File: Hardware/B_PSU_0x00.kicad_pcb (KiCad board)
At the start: 2 copper layers, 111.8 x 73.7 mm, 95 parts, among them J1 Conn_01x03, J10 Conn_01x02, J11 Conn_01x02, J12 Conn_01x02, J13 Conn_01x02, J14 Conn_01x02, J15 Conn_01x03, J16 Conn_01x03, J17 Conn_01x03, J18 Conn_01x04, J19 Conn_01x04, J2 Conn_01x04, J3 Conn_01x04, J4 Conn_01x02, J5 Conn_01x02, J6 Conn_01x02, J7 Conn_01x03, J8 Conn_01x02, J9 Conn_01x03, U1 ADP5070AREZ, U2 ADP7142AUJZ-5.0, U3 ADP7142AUJZ-3.3, U4 ADP7142AUJZ-1.8, U5 ADP7182AUJZ-1.8, U6 ADP7142AUJZ-2.5, U7 ADP7183ACPZN3.3-R7

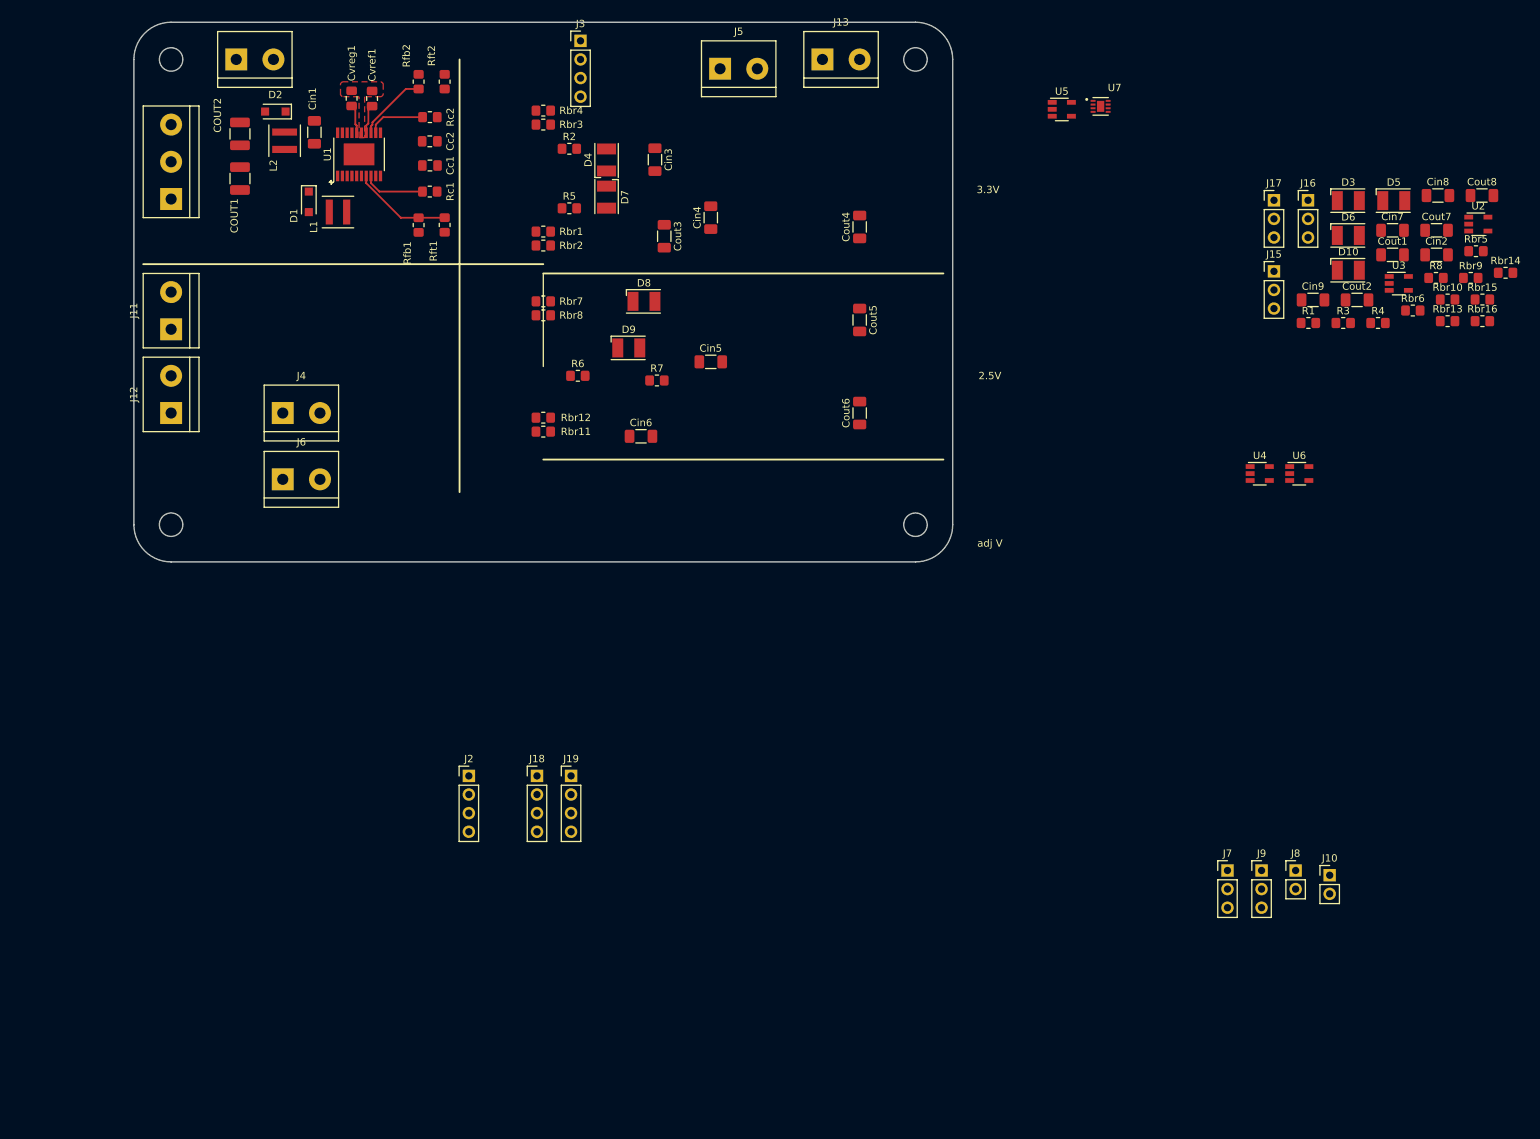
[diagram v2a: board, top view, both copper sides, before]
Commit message: updated to sch and pcb
correct LDO ic's and board outline
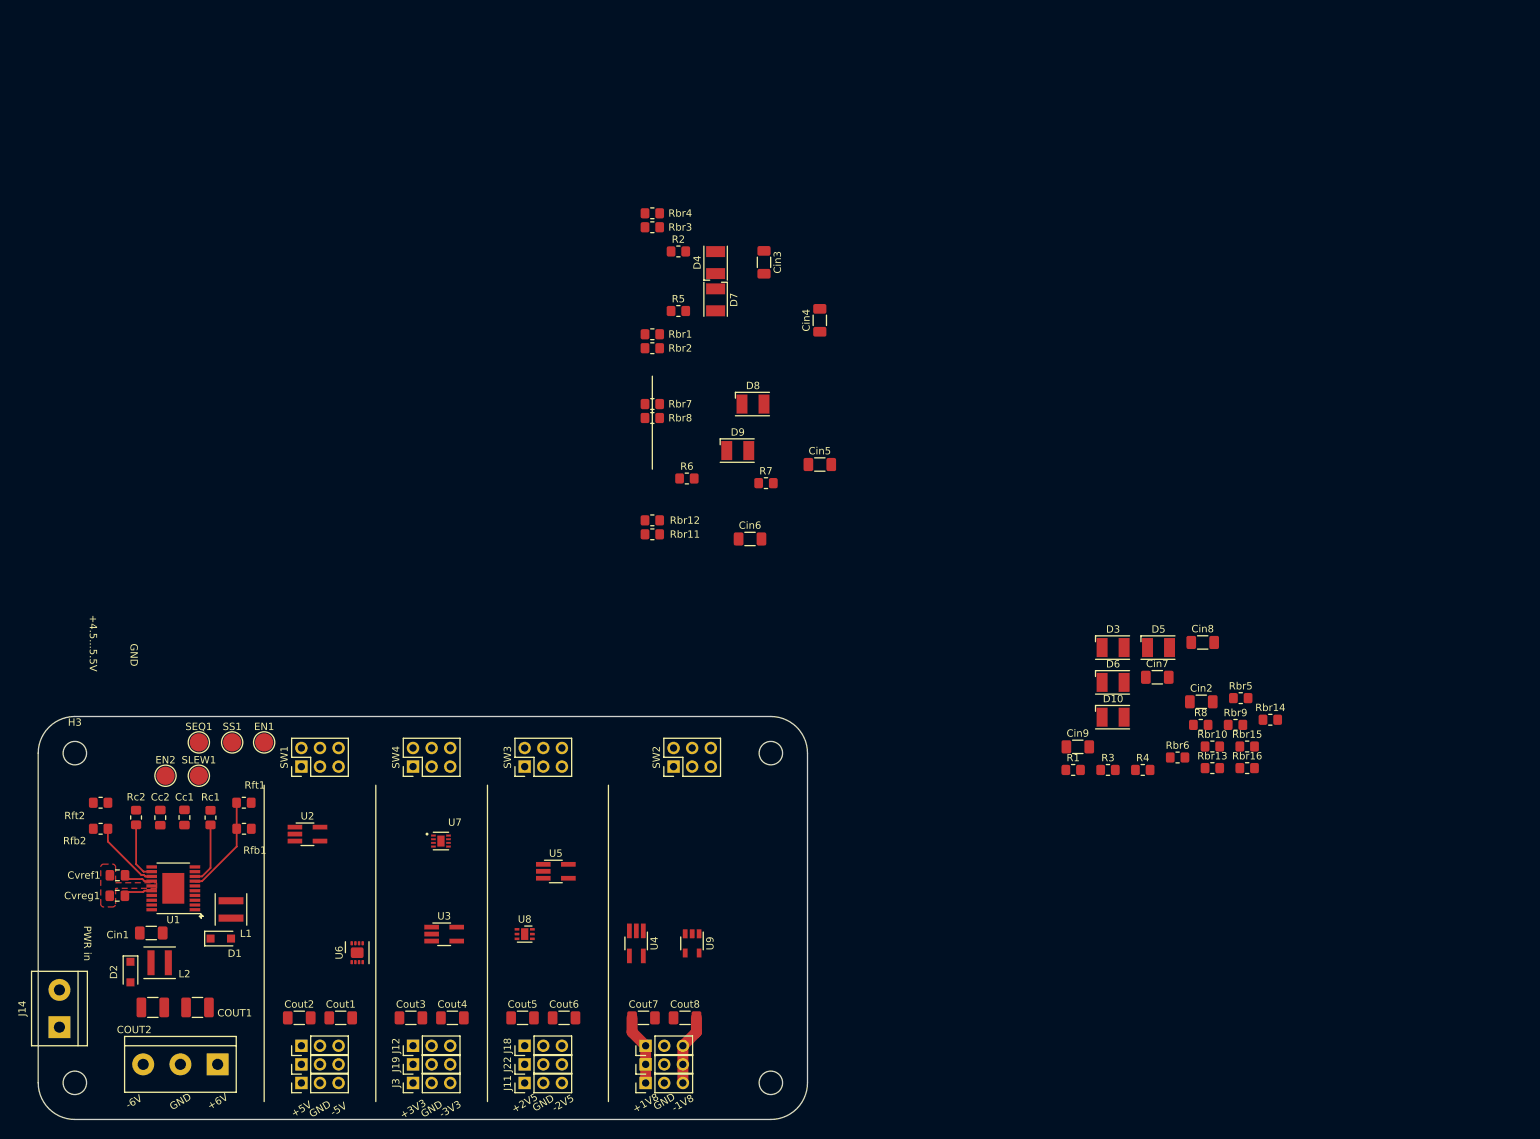
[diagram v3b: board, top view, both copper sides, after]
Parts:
- removed H5: MountingHole, MountingHole:MountingHole_3.2mm_M3
- removed J10, J8: Conn_01x02, Connector_PinHeader_2.54mm:PinHeader_1x02_P2.54mm_Vertical
- removed J15, J16, J17, J7, J9: Conn_01x03, Connector_PinHeader_2.54mm:PinHeader_1x03_P2.54mm_Vertical
- removed J2: Conn_01x04, Connector_PinHeader_2.54mm:PinHeader_1x04_P2.54mm_Vertical
- added EN1: TestPoint, TestPoint:TestPoint_Pad_D2.5mm, F.Cu at (53.3, 113.5)
- added EN2: TestPoint, TestPoint:TestPoint_Pad_D2.5mm, F.Cu at (39.9, 118.1)
- added H3: MountingHole, MountingHole:MountingHole_3.2mm_M3, F.Cu at (27.5, 115.0)
- added J20: Conn_01x03, Connector_PinHeader_2.54mm:PinHeader_1x03_P2.54mm_Vertical, F.Cu at (58.4, 154.9)
- added J21: Conn_01x03, Connector_PinHeader_2.54mm:PinHeader_1x03_P2.54mm_Vertical, F.Cu at (105.4, 154.9)
- added J22: Conn_01x03, Connector_PinHeader_2.54mm:PinHeader_1x03_P2.54mm_Vertical, F.Cu at (88.9, 157.5)
- added SEQ1: TestPoint, TestPoint:TestPoint_Pad_D2.5mm, F.Cu at (44.4, 113.5)
- added SLEW1: TestPoint, TestPoint:TestPoint_Pad_D2.5mm, F.Cu at (44.4, 118.1)
- added SS1: TestPoint, TestPoint:TestPoint_Pad_D2.5mm, F.Cu at (49.0, 113.5)
- added SW1: SW_DPDT_x2, Connector_PinHeader_2.54mm:PinHeader_2x03_P2.54mm_Vertical, F.Cu at (58.4, 116.8)
- added SW2: SW_DPDT_x2, Connector_PinHeader_2.54mm:PinHeader_2x03_P2.54mm_Vertical, F.Cu at (109.2, 116.8)
- added SW3: SW_DPDT_x2, Connector_PinHeader_2.54mm:PinHeader_2x03_P2.54mm_Vertical, F.Cu at (88.9, 116.8)
- added SW4: SW_DPDT_x2, Connector_PinHeader_2.54mm:PinHeader_2x03_P2.54mm_Vertical, F.Cu at (73.7, 116.8)
- added U8: ADP7182ACPZN-2.5R7, Package_DFN_QFN:DFN-6-1EP_2x2mm_P0.65mm_EP1x1.6mm, F.Cu at (88.9, 139.7)
- added U9: ADP7182AUJZ-1.8, Package_TO_SOT_SMD:TSOT-23-5, F.Cu at (111.8, 141.0)
- Cin4: value 10uF -> 4.7uF
- Cout4: value 2.2uF -> 4.7uF
- J11, J12, J13, J4, J5, J6: value Conn_01x02 -> Conn_01x03; footprint TerminalBlock:TerminalBlock_bornier-2_P5.08mm -> Connector_PinHeader_2.54mm:PinHeader_1x03_P2.54mm_Vertical
- J18, J19, J3: value Conn_01x04 -> Conn_01x03; footprint Connector_PinHeader_2.54mm:PinHeader_1x04_P2.54mm_Vertical -> Connector_PinHeader_2.54mm:PinHeader_1x03_P2.54mm_Vertical
- U2: value ADP7142AUJZ-5.0 -> ADP7118WAUJZ-5.0; footprint Package_TO_SOT_SMD:TSOT-23-5 -> Package_TO_SOT_SMD:TSOT-23-5_HandSoldering
- U3: value ADP7142AUJZ-3.3 -> ADP7118AUJZ-3.3-R7; footprint Package_TO_SOT_SMD:TSOT-23-5 -> Package_TO_SOT_SMD:TSOT-23-5_HandSoldering
- U4: footprint Package_TO_SOT_SMD:TSOT-23-5 -> Package_TO_SOT_SMD:TSOT-23-5_HandSoldering
- U5: value ADP7182AUJZ-1.8 -> ADP7118AUJZ-2.5-R7; footprint Package_TO_SOT_SMD:TSOT-23-5 -> Package_TO_SOT_SMD:TSOT-23-5_HandSoldering
- U6: value ADP7142AUJZ-2.5 -> ADP7182ACPZ-5.0-R7; footprint Package_TO_SOT_SMD:TSOT-23-5 -> Package_CSP:LFCSP-8-1EP_3x3mm_P0.5mm_EP1.45x1.74mm
- moved U2 180.2 mm to (59.2, 126.0)
- moved Cout1 177.4 mm to (63.8, 151.1)
- moved Cout2 174.5 mm to (58.1, 151.1)
- moved U3 157.7 mm to (77.9, 139.7)
- moved Cout8 156.3 mm to (110.8, 151.1)
- moved Cout7 152.5 mm to (105.1, 151.1)
- moved U6 144.3 mm to (66.0, 142.2), turned to 90 degrees
- moved J3 144.1 mm to (73.7, 160.0), turned to 90 degrees
- moved H1 141.1 mm to (122.5, 160.0)
- moved J13 139.3 mm to (105.4, 157.5), turned to 90 degrees
- moved J5 138.8 mm to (105.4, 160.0), turned to 90 degrees
- moved U7 134.8 mm to (77.5, 127.0)
- moved J14 134.3 mm to (25.4, 152.4), turned to 90 degrees
- moved U5 124.8 mm to (93.2, 131.1)
- moved Cout4 121.4 mm to (79.0, 151.1), turned to 0 degrees
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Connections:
- COUT1 pad 1: GNDREF -> GNDA
- COUT2 pad 2: GNDREF -> GNDA
- Cin1 pad 2: GNDREF -> GNDA
- Cin7 pad 1: (no net) -> GNDA
- Cin7 pad 2: (no net) -> Net-(Cin7-Pad2)
- Cin9 pad 1: (no net) -> GNDA
- Cin9 pad 2: (no net) -> Net-(Cin9-Pad2)
- Cout1 pad 1: (no net) -> Net-(Cout1-Pad1)
- Cout1 pad 2: Net-(Cout1-Pad2) -> /-5V
- Cout2 pad 1: Net-(Cout2-Pad1) -> /+5V
- Cout2 pad 2: (no net) -> Net-(Cout1-Pad1)
- Cout3 pad 1: Net-(Cout3-Pad1) -> /+3v3
- Cout4 pad 2: Net-(Cout4-Pad2) -> /-3v3
- Cout5 pad 1: Net-(Cout5-Pad1) -> /+2v5
- Cout6 pad 2: Net-(Cout6-Pad2) -> /-2v5
- Cout7 pad 1: Net-(Cout7-Pad1) -> /+1v8
- Cout8 pad 1: (no net) -> GNDA
- Cout8 pad 2: Net-(Cout8-Pad2) -> /-1v8
- J1 pad 2: GNDREF -> GNDA
- J11 pad 1: Net-(Cout7-Pad1) -> /+2v5
- J12 pad 1: Net-(Cout8-Pad2) -> /+3v3
- J12 pad 2: (no net) -> GNDA
- J13 pad 1: Net-(Cout6-Pad2) -> /+1v8
- J14 pad 2: GNDREF -> GNDA
- J18 pad 1: (no net) -> /+2v5
- J18 pad 2: (no net) -> GNDA
- J18 pad 3: (no net) -> /-2v5
- J19 pad 1: (no net) -> /+3v3
- J19 pad 2: (no net) -> GNDA
- J19 pad 3: (no net) -> /-3v3
- J3 pad 1: Net-(Cout3-Pad1) -> /+3v3
- J3 pad 3: GNDA -> /-3v3
- J4 pad 1: Net-(Cout2-Pad1) -> /+5V
- J4 pad 2: (no net) -> Net-(Cout1-Pad1)
- J5 pad 1: Net-(Cout5-Pad1) -> /+1v8
- J6 pad 1: Net-(Cout1-Pad2) -> /+5V
- J6 pad 2: (no net) -> Net-(Cout1-Pad1)
- L2 pad 2: GNDREF -> GNDA
- R3 pad 1: (no net) -> Net-(Cin7-Pad2)
- R8 pad 1: (no net) -> Net-(Cin9-Pad2)
- Rbr1 pad 2: /Vneg -> Net-(Rbr1-Pad2)
- Rbr15 pad 1: Net-(Rbr15-Pad1) -> Net-(Cin9-Pad2)
- Rbr16 pad 1: Net-(Rbr15-Pad1) -> Net-(Cin9-Pad2)
- Rbr2 pad 2: /Vneg -> Net-(Rbr1-Pad2)
- Rbr5 pad 1: Net-(Rbr5-Pad1) -> Net-(Cin7-Pad2)
- Rbr6 pad 1: Net-(Rbr5-Pad1) -> Net-(Cin7-Pad2)
- U1 pad 1: GNDREF -> GNDA
- U1 pad 10: (no net) -> Net-(SS1-Pad1)
- U1 pad 11: (no net) -> Net-(EN2-Pad1)
- U1 pad 5: (no net) -> Net-(SEQ1-Pad1)
- U1 pad 6: (no net) -> Net-(SLEW1-Pad1)
- U1 pad 9: (no net) -> Net-(EN1-Pad1)
- U2 pad 3: Net-(J15-Pad2) -> /EN_+5v
- U2 pad 4: (no net) -> /+5V
- U2 pad 5: Net-(Cout2-Pad1) -> /+5V
- U3 pad 3: Net-(J9-Pad2) -> /EN_+3v3
- U3 pad 4: Net-(Cout3-Pad1) -> /+3v3
- U3 pad 5: Net-(Cout3-Pad1) -> /+3v3
- U4 pad 3: Net-(J16-Pad2) -> /EN_+1v8
- U4 pad 4: Net-(Cout7-Pad1) -> /+1v8
- U4 pad 5: Net-(Cout7-Pad1) -> /+1v8
- U5 pad 1: (no net) -> Net-(Cin5-Pad1)
- U5 pad 2: (no net) -> GNDA
- U5 pad 3: (no net) -> /EN_+2v5
- U5 pad 4: (no net) -> /+2v5
- U5 pad 5: (no net) -> /+2v5
- U6 pad 1: Net-(Cin5-Pad1) -> /-5V
- U6 pad 2: GNDA -> /-5V
- U6 pad 3: Net-(J17-Pad2) -> /EN_-5v
- U6 pad 4: Net-(Cout5-Pad1) -> (no net)
- U6 pad 5: Net-(Cout5-Pad1) -> (no net)
- U7 pad 1: (no net) -> /-3v3
- U7 pad 2: (no net) -> /-3v3
- U7 pad 5: (no net) -> /EN_-3v3
- U7 pad 6: (no net) -> GNDA
- U7 pad 8: (no net) -> Net-(Cin4-Pad1)
- U7 pad 9: (no net) -> Net-(Cin4-Pad1)
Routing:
- net /-1v8: track 0.00 -> 9.66 mm
- net /+1v8: track 0.00 -> 9.66 mm
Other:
- board size 111.8 x 73.7 mm -> 105 x 55 mm
- board text added: "+1V8"
- board text added: "+2V5"
- board text added: "+3V3"
- board text added: "+4.5...5.5V"
- board text added: "+5V"
- board text added: "+6V"
- board text added: "-1V8"
- board text added: "-2V5"
- board text added: "-3V3"
- board text added: "-5V"
- board text added: "-6V"
- board text added: "GND"
- board text added: "PWR in"
- board text removed: "2.5V"
- board text removed: "3.3V"
- board text removed: "adj V"

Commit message: WIP
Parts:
- removed D10, D3, D4, D5, D6, D7, D8, D9: LED, LED_SMD:LED_PLCC-2
- removed R1, R2, R3, R4, R5, R6, R7, R8, Rbr1, Rbr10, Rbr11, Rbr12, Rbr13, Rbr14, Rbr15, Rbr16, Rbr2, Rbr3, Rbr4, Rbr5, Rbr6, Rbr7, Rbr8, Rbr9: 0R, Resistor_SMD:R_0805_2012Metric_Pad1.20x1.40mm_HandSolder
- removed SW1, SW2, SW3, SW4: SW_DPDT_x2, Connector_PinHeader_2.54mm:PinHeader_2x03_P2.54mm_Vertical
- added Ca1: 1uF, Capacitor_SMD:C_1206_3216Metric_Pad1.33x1.80mm_HandSolder, F.Cu at (110.0, 101.6)
- added Cafb1: 10nF, Capacitor_SMD:C_1206_3216Metric_Pad1.33x1.80mm_HandSolder, F.Cu at (116.0, 101.6)
- added Creg1: 1uF, Capacitor_SMD:C_1206_3216Metric_Pad1.33x1.80mm_HandSolder, F.Cu at (117.1, 106.2)
- added J10: Conn_01x02, Connector_PinHeader_2.54mm:PinHeader_1x02_P2.54mm_Vertical, F.Cu at (115.0, 92.2)
- added J15: Conn_01x02, Connector_PinHeader_2.54mm:PinHeader_1x02_P2.54mm_Vertical, F.Cu at (130.2, 92.2)
- added J16: Conn_01x02, Connector_PinHeader_2.54mm:PinHeader_1x02_P2.54mm_Vertical, F.Cu at (140.3, 92.2)
- added J17: Conn_01x02, Connector_PinHeader_2.54mm:PinHeader_1x02_P2.54mm_Vertical, F.Cu at (125.1, 92.2)
- added J2: Conn_01x02, Connector_PinHeader_2.54mm:PinHeader_1x02_P2.54mm_Vertical, F.Cu at (99.7, 92.2)
- added J23: Conn_01x02, Connector_PinHeader_2.54mm:PinHeader_1x02_P2.54mm_Vertical, F.Cu at (97.2, 92.2)
- added J24: Conn_01x02, Connector_PinHeader_2.54mm:PinHeader_1x02_P2.54mm_Vertical, F.Cu at (142.9, 92.2)
- added J25: Conn_01x02, Connector_PinHeader_2.54mm:PinHeader_1x02_P2.54mm_Vertical, F.Cu at (112.4, 92.2)
- added J26: Conn_01x02, Connector_PinHeader_2.54mm:PinHeader_1x02_P2.54mm_Vertical, F.Cu at (127.7, 92.2)
- added J27: Conn_01x03, Connector_PinHeader_2.54mm:PinHeader_1x03_P2.54mm_Vertical, F.Cu at (81.2, 127.0)
- added J28: Conn_01x03, Connector_PinHeader_2.54mm:PinHeader_1x03_P2.54mm_Vertical, F.Cu at (81.2, 130.1)
- added J7: Conn_01x02, Connector_PinHeader_2.54mm:PinHeader_1x02_P2.54mm_Vertical, F.Cu at (94.6, 92.2)
- added J8: Conn_01x02, Connector_PinHeader_2.54mm:PinHeader_1x02_P2.54mm_Vertical, F.Cu at (145.4, 92.2)
- added J9: Conn_01x02, Connector_PinHeader_2.54mm:PinHeader_1x02_P2.54mm_Vertical, F.Cu at (109.9, 92.2)
- EN1, EN2, SEQ1, SLEW1, SS1: moved to B.Cu
- J1: footprint TerminalBlock:TerminalBlock_bornier-3_P5.08mm -> Connector_PinHeader_2.54mm:PinHeader_1x03_P2.54mm_Vertical
- moved Cin2 86.0 mm to (95.3, 106.2)
- moved Cin7 73.0 mm to (102.2, 106.2)
- moved Cin3 58.7 mm to (112.1, 105.9)
- moved Cin4 58.7 mm to (119.7, 113.9)
- moved U8 54.0 mm to (134.0, 110.0), turned to 90 degrees
- moved J14 49.6 mm to (64.2, 121.4)
- moved Rfb2 49.4 mm to (69.6, 94.5)
- moved Rft2 49.4 mm to (69.6, 90.9)
- moved Cout6 49.0 mm to (132.1, 119.9)
- moved Cout4 48.8 mm to (116.5, 119.9)
- moved Cout9 48.8 mm to (95.6, 119.9)
- moved Cout10 48.8 mm to (101.3, 119.9)
- moved Cout3 48.8 mm to (110.8, 119.9)
- moved Cin1 48.6 mm to (75.4, 108.6)
- moved J3 48.6 mm to (111.1, 129.1)
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- renumbered Cout1 to Cout10, Cout2 to Cout9
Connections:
- Cin2 pad 1: Net-(Cin2-Pad1) -> /EN_+5v
- Cin2 pad 2: GNDA -> Net-(Cin2-Pad2)
- Cin3 pad 1: Net-(Cin3-Pad1) -> /EN_+3v3
- Cin3 pad 2: GNDA -> Net-(Cin3-Pad2)
- Cin4 pad 1: Net-(Cin4-Pad1) -> /EN_-3v3
- Cin4 pad 2: GNDA -> Net-(Cin3-Pad2)
- Cin5 pad 1: Net-(Cin5-Pad1) -> /EN_+2v5
- Cin5 pad 2: GNDA -> Net-(Cin5-Pad2)
- Cin6 pad 1: Net-(Cin6-Pad1) -> /EN_-2v5
- Cin6 pad 2: GNDA -> Net-(Cin5-Pad2)
- Cin7 pad 1: GNDA -> Net-(Cin2-Pad2)
- Cin7 pad 2: Net-(Cin7-Pad2) -> /EN_-5v
- Cin8 pad 1: Net-(Cin8-Pad1) -> /EN_+1v8
- Cin8 pad 2: GNDA -> Net-(Cin8-Pad2)
- Cin9 pad 1: GNDA -> Net-(Cin8-Pad2)
- Cin9 pad 2: Net-(Cin9-Pad2) -> /EN_-1v8
- Cout10 pad 1: Net-(Cout1-Pad1) -> Net-(Cin2-Pad2)
- Cout3 pad 2: GNDA -> Net-(Cin3-Pad2)
- Cout4 pad 1: GNDA -> Net-(Cin3-Pad2)
- Cout5 pad 2: GNDA -> Net-(Cin5-Pad2)
- Cout6 pad 1: GNDA -> Net-(Cin5-Pad2)
- Cout7 pad 2: GNDA -> Net-(Cin8-Pad2)
- Cout8 pad 1: GNDA -> Net-(Cin8-Pad2)
- Cout9 pad 2: Net-(Cout1-Pad1) -> Net-(Cin2-Pad2)
- J11 pad 2: GNDA -> Net-(Cin5-Pad2)
- J12 pad 2: GNDA -> Net-(Cin3-Pad2)
- J13 pad 2: GNDA -> Net-(Cin8-Pad2)
- J18 pad 2: GNDA -> Net-(Cin5-Pad2)
- J19 pad 2: GNDA -> Net-(Cin3-Pad2)
- J20 pad 2: Net-(Cout1-Pad1) -> Net-(Cin2-Pad2)
- J21 pad 2: GNDA -> Net-(Cin8-Pad2)
- J22 pad 2: GNDA -> Net-(Cin5-Pad2)
- J3 pad 2: GNDA -> Net-(Cin3-Pad2)
- J4 pad 2: Net-(Cout1-Pad1) -> Net-(Cin2-Pad2)
- J5 pad 2: GNDA -> Net-(Cin8-Pad2)
- J6 pad 2: Net-(Cout1-Pad1) -> Net-(Cin2-Pad2)
- U2 pad 1: Net-(Cin2-Pad1) -> /EN_+5v
- U2 pad 2: GNDA -> Net-(Cin2-Pad2)
- U3 pad 1: Net-(Cin3-Pad1) -> /EN_+3v3
- U3 pad 2: GNDA -> Net-(Cin3-Pad2)
- U4 pad 1: Net-(Cin8-Pad1) -> /EN_+1v8
- U4 pad 2: GNDA -> Net-(Cin8-Pad2)
- U5 pad 1: Net-(Cin5-Pad1) -> /EN_+2v5
- U5 pad 2: GNDA -> Net-(Cin5-Pad2)
- U6 pad 3: /EN_-5v -> unconnected-(U6-Pad3)
- U6 pad 4: (no net) -> /EN_-5v
- U6 pad 5: (no net) -> unconnected-(U6-Pad5)
- U6 pad 6: GNDA -> Net-(Cin2-Pad2)
- U6 pad 7: Net-(Cin7-Pad2) -> /EN_-5v
- U6 pad 8: Net-(Cin7-Pad2) -> /EN_-5v
- U6 pad 9: Net-(Cin7-Pad2) -> /EN_-5v
- U7 pad 6: GNDA -> Net-(Cin3-Pad2)
- U8 pad 2: (no net) -> unconnected-(U8-Pad2)
- U8 pad 4: (no net) -> unconnected-(U8-Pad4)
- U8 pad 5: GNDA -> Net-(Cin5-Pad2)
- U8 pad 6: Net-(Cin6-Pad1) -> /EN_-2v5
- U8 pad 7: Net-(Cin6-Pad1) -> /EN_-2v5
- U9 pad 1: GNDA -> Net-(Cin8-Pad2)
- U9 pad 2: Net-(Cin9-Pad2) -> /EN_-1v8
- U9 pad 4: (no net) -> unconnected-(U9-Pad4)
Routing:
- net /-2v5: track 0.00 -> 10.2 mm
- net /-3v3: track 0.00 -> 9.91 mm
- net /+2v5: track 0.00 -> 9.91 mm
- net /-1v8: track 9.66 -> 0.00 mm
- net /+1v8: track 9.66 -> 0.00 mm
- net Net-(D1-Pad2): track 0.00 -> 5.67 mm
- net Net-(L1-Pad1): track 0.00 -> 4.95 mm
- net /+5V: track 0.00 -> 0.64 mm
- net Net-(Cin8-Pad2): vias 0 -> 4
- net Net-(Cin5-Pad2): vias 0 -> 4
- net GNDA: vias 0 -> 22
- net /Vpoz: vias 0 -> 1
- net /Vneg: vias 0 -> 1
- added copper zone on F.Cu, net +VDC
- added copper zone on F.Cu, net /+3v3
- added copper zone on F.Cu, net /+5V
- added copper zone on F.Cu, net /-5V
- added copper zone on F.Cu, net /EN_-5v
- added copper zone on F.Cu, net /Vneg
- added copper zone on F.Cu, net /Vpoz
- added copper zone on B.Cu, net GNDA
- added copper zone on F.Cu, net Net-(Cin2-Pad2)
- added copper zone on F.Cu, net Net-(Cin3-Pad2)
- added copper zone on B.Cu, net Net-(Cin5-Pad2)
- added copper zone on F.Cu, net Net-(Cin5-Pad2)
- added copper zone on B.Cu, net Net-(Cin8-Pad2)
- added copper zone on F.Cu, net Net-(Cin8-Pad2)
- added copper zone on F.Cu, net Net-(D1-Pad2)
- added copper zone on F.Cu, net Net-(D2-Pad1)
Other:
- board size 105 x 55 mm -> 101.1 x 52.5 mm
- net class Default removed
- board text removed: "+4.5...5.5V"

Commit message: cleaned up layout
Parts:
- moved EN2 18.8 mm to (72.9, 85.6)
- moved SLEW1 18.2 mm to (86.9, 85.6)
- moved SEQ1 13.2 mm to (92.5, 85.1)
- moved EN1 12.2 mm to (82.3, 85.6)
- moved SS1 11.6 mm to (77.5, 85.6)
- moved Cin4 4.56 mm to (115.1, 113.8), turned to -90 degrees
- moved Rft1 4.19 mm to (88.1, 95.0)
- moved Cin9 3.88 mm to (149.2, 108.8), turned to 0 degrees
- moved Rfb1 3.39 mm to (87.5, 91.0), turned to 180 degrees
- moved U9 3.13 mm to (149.1, 113.1), turned to 180 degrees
- moved Cin3 2.53 mm to (109.7, 106.9), turned to 0 degrees
- moved U7 1.95 mm to (118.9, 111.3)
- moved U4 1.18 mm to (141.0, 113.5), turned to 180 degrees
- moved Creg1 0.83 mm to (117.6, 105.5), turned to 180 degrees
- moved Ca1 0.48 mm to (110.5, 101.6), turned to 180 degrees
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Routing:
- net Net-(Cin8-Pad2): track 0.00 -> 38.9 mm
- net /Vneg: track 0.00 -> 29.6 mm, vias 1 -> 2
- net Net-(Cin2-Pad2): track 0.00 -> 24.2 mm, vias 0 -> 2
- net Net-(SEQ1-Pad1): track 0.00 -> 24.2 mm, vias 0 -> 1
- net /EN_+1v8: track 0.00 -> 23.6 mm
- net /Vpoz: track 0.00 -> 21.5 mm
- net /EN_-1v8: track 0.00 -> 20.7 mm
- net /EN_+5v: track 0.00 -> 20.7 mm
- net Net-(SLEW1-Pad1): track 0.00 -> 19.8 mm, vias 0 -> 1
- net Net-(EN1-Pad1): track 0.00 -> 16.2 mm, vias 0 -> 1
- net Net-(SS1-Pad1): track 0.00 -> 15.7 mm, vias 0 -> 1
- net Net-(EN2-Pad1): track 0.00 -> 15.0 mm, vias 0 -> 1
- net /EN_-5v: track 0.00 -> 14.7 mm
- net GNDA: track 0.00 -> 12.9 mm, vias 22 -> 23
- net Net-(Cvref1-Pad2): track 3.97 -> 11.5 mm
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- removed copper zone on B.Cu, net Net-(Cin5-Pad2)
- removed copper zone on B.Cu, net Net-(Cin8-Pad2)
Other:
- outline, holes or cut-outs redrawn
